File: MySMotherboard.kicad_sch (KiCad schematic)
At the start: 53 parts, among them SW1 RST, SW2 BTN, U1 MCP1640Cx-xCHY, U2 APE8865Y5-30-HF-3, U3 ATmega328PB-A, U4 AT25xxx, U5 RFM69HW, U6 ATSHA204A, U7 AP63205WU, U8 SP3481EN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

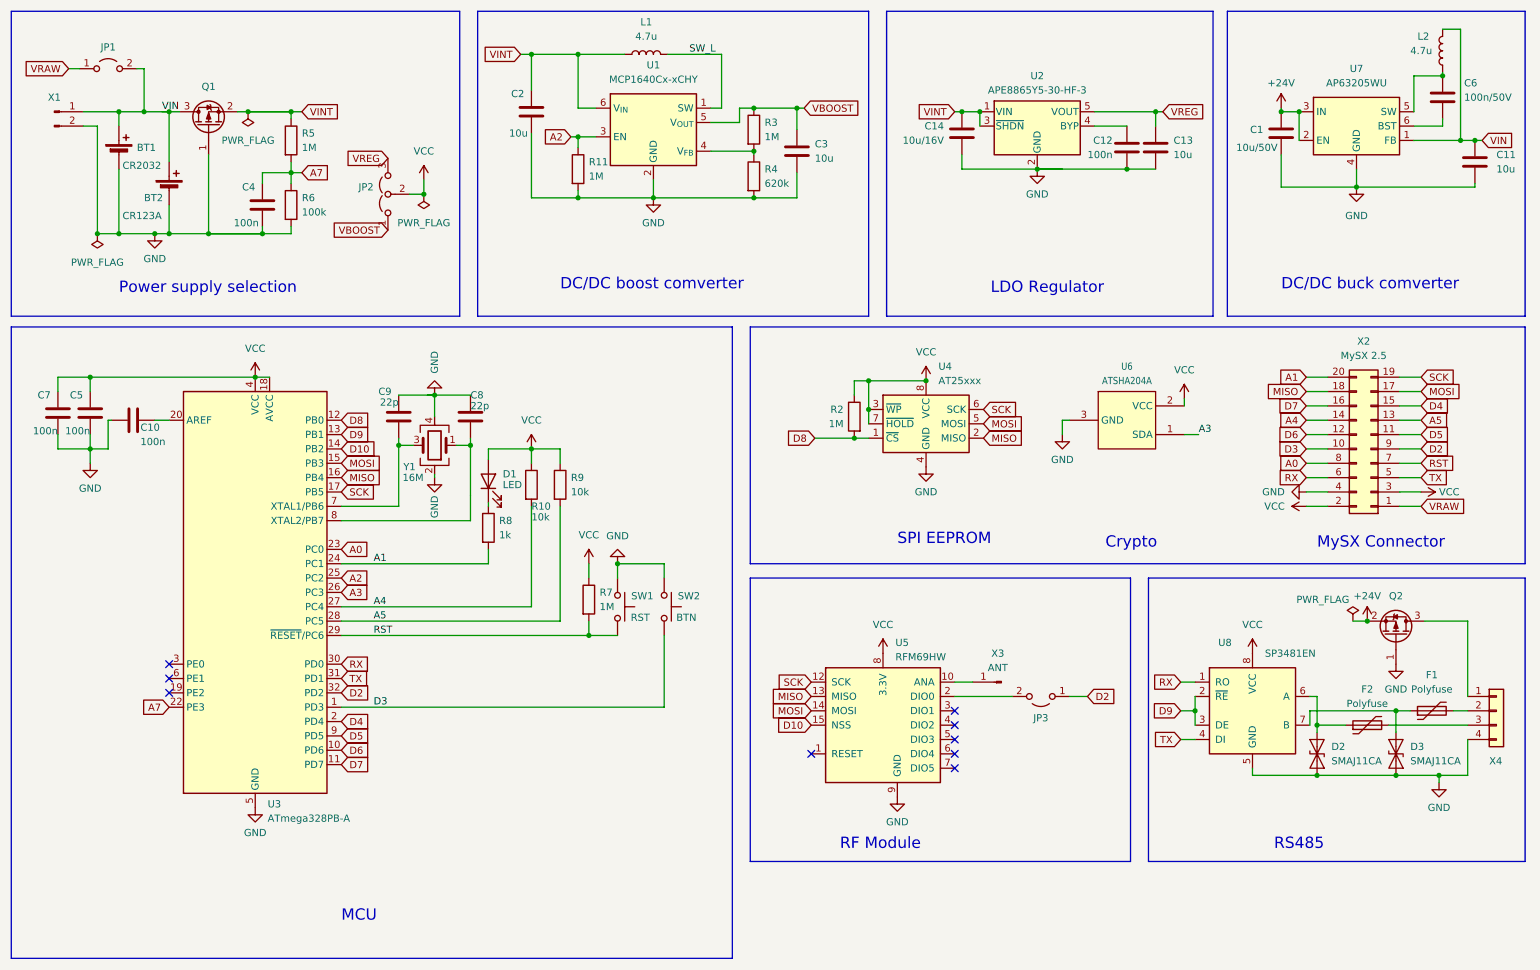
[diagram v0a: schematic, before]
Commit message: update to kicad 8
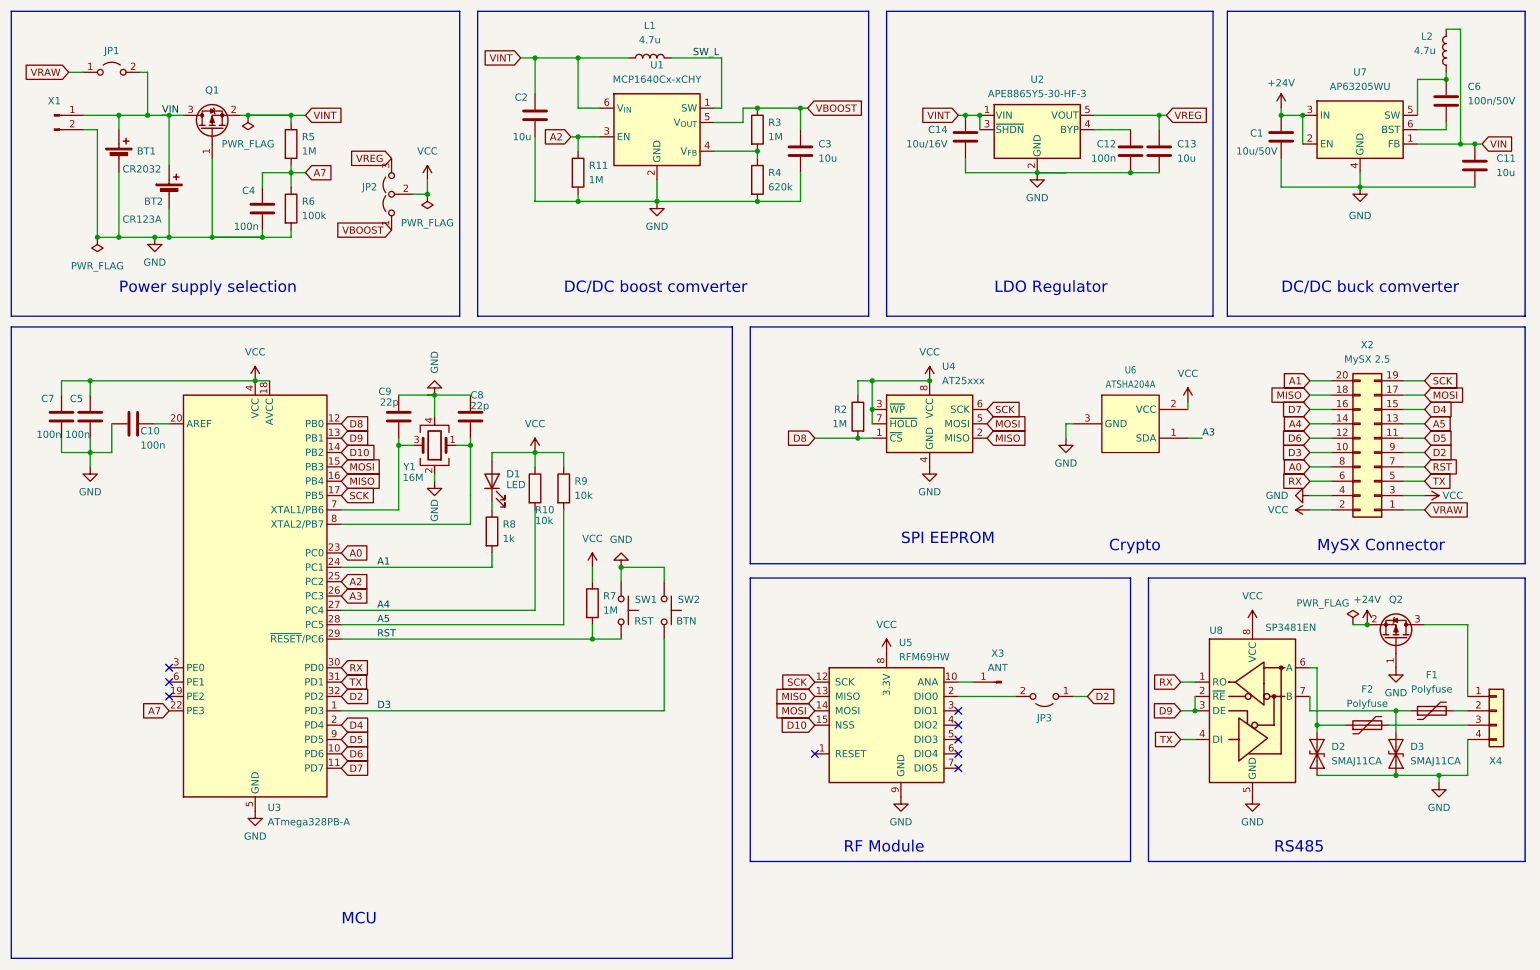
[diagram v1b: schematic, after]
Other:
- moved on the sheet: BT1, BT2, C1, C10, C11, C12, C13, C14, C2, C3, C4, C5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

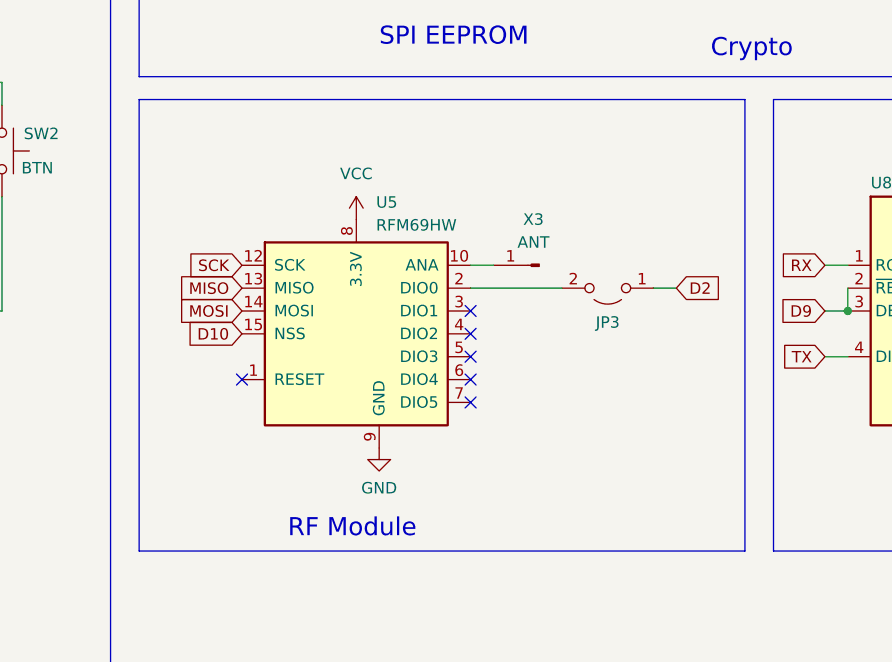
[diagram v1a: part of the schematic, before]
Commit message: add pull-up resistor for RFM69W NSS pin
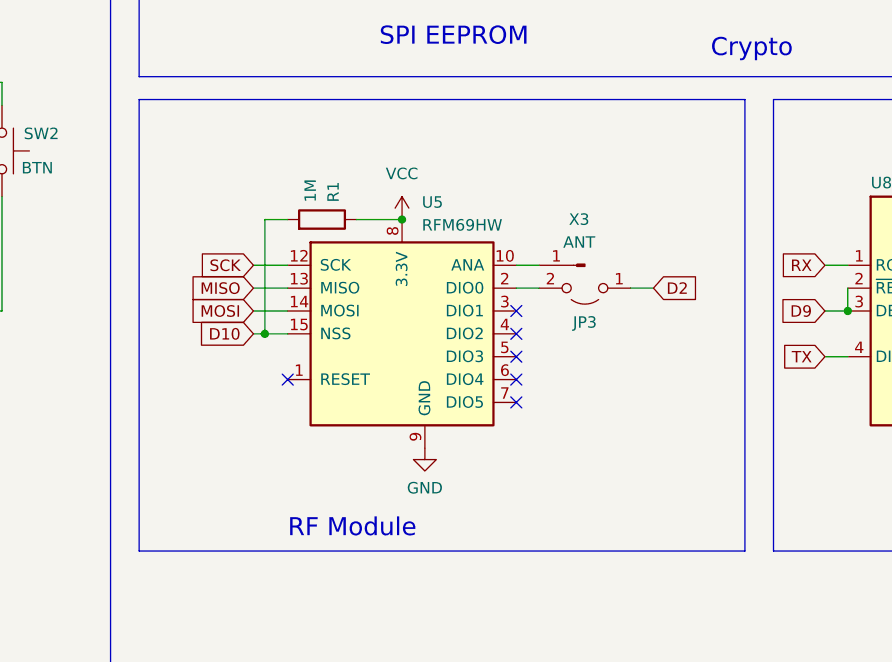
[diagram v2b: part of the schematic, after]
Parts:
- added R1: 1M, Resistor_SMD:R_0603_1608Metric, symbol Device:R
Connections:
- net D10: now also R1.2
- net VCC: now also R1.1
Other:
- moved on the sheet: JP3, U5, X3

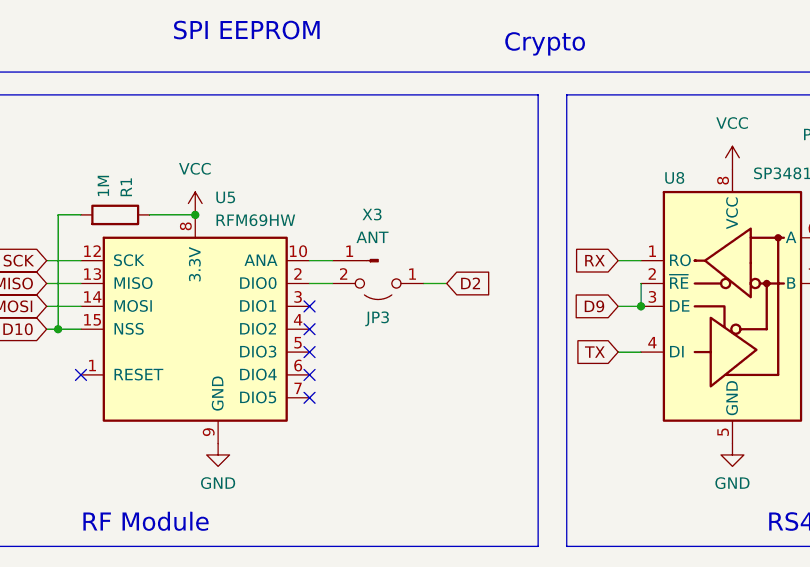
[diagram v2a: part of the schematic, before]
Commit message: add option to connect RFM69W irq to pin 3
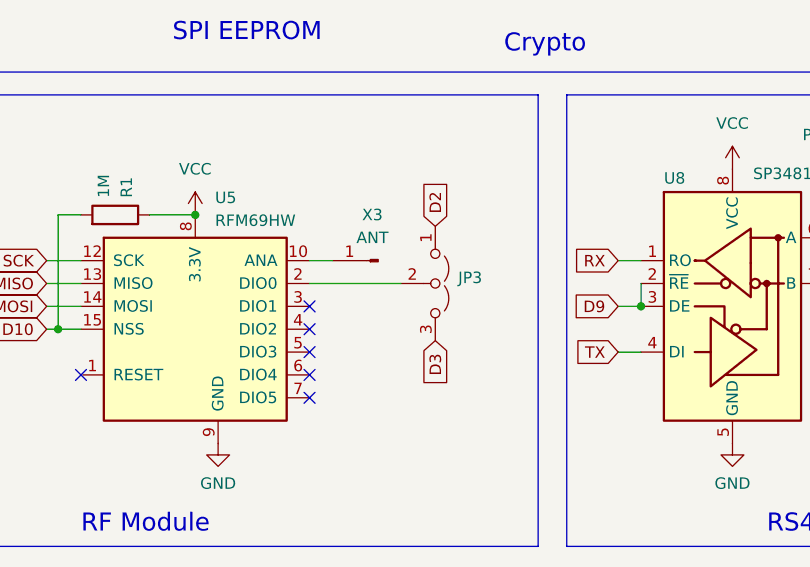
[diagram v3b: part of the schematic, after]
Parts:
- removed JP3: ~, Jumper:SolderJumper-2_P1.3mm_Open_RoundedPad1.0x1.5mm, symbol Jumper:Jumper_2_Open
- added JP3: ~, Jumper:SolderJumper-3_P1.3mm_Open_RoundedPad1.0x1.5mm, symbol Jumper:Jumper_3_Open
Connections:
- net D2: now also JP3.1 (A)
- net D3: now also JP3.3 (B)
- net at U5.2 (DIO0): now also JP3.2 (C)
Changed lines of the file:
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@@
 	(wire
 		(pts
-			(xy 199.39 134.62) (xy 201.93 134.62)
-		)
-		(stroke
-			(width 0)
-			(type default)
-		)
-	)
-	(wire
-		(pts
 			(xy 40.64 31.75) (xy 41.91 31.75)
 		)
@@
 	(wire
 		(pts
-			(xy 186.69 134.62) (xy 189.23 134.62)
+			(xy 186.69 134.62) (xy 196.85 134.62)
 		)
 		(stroke
@@
 	(global_label "D2"
 		(shape input)
-		(at 201.93 134.62 0)
+		(at 200.66 128.27 90)
 		(fields_autoplaced yes)
 		(effects
@@
 		)
 		(property "Intersheetrefs" "${INTERSHEET_REFS}"
-			(at 207.3947 134.62 0)
+			(at 200.66 122.8053 90)
 			(effects
 				(font
@@
 		)
 	)
+	(global_label "D3"
+		(shape input)
+		(at 200.66 140.97 270)
+		(fields_autoplaced yes)
+		(effects
+			(font
+				(size 1.27 1.27)
+			)
+			(justify right)
+		)
+		(property "Intersheetrefs" "${INTERSHEET_REFS}"
+			(at 200.66 146.4347 90)
+			(effects
+				(font
+					(size 1.27 1.27)
+				)
+				(justify right)
+				(hide yes)
+			)
+		)
+	)
 	(global_label "A5"
 		(shape input)
@@
 	)
 	(symbol
-		(lib_id "Jumper:Jumper_2_Open")
-		(at 194.31 134.62 180)
-		(unit 1)
-		(exclude_from_sim no)
-		(in_bom yes)
-		(on_board yes)
-		(dnp no)
-		(property "Reference" "JP3"
-			(at 194.31 138.43 0)
-			(effects
-				(font
-					(size 1.27 1.27)
-				)
-			)
-		)
-		(property "Value" "~"
-			(at 194.31 138.43 0)
-			(effects
-				(font
-					(size 1.27 1.27)
-				)
-			)
-		)
-		(property "Footprint" "Jumper:SolderJumper-2_P1.3mm_Open_RoundedPad1.0x1.5mm"
-			(at 194.31 134.62 0)
-			(effects
-				(font
-					(size 1.27 1.27)
-				)
-				(hide yes)
-			)
-		)
-		(property "Datasheet" "~"
-			(at 194.31 134.62 0)
-			(effects
-				(font
-					(size 1.27 1.27)
-				)
-				(hide yes)
-			)
-		)
-		(property "Description" ""
-			(at 194.31 134.62 0)
-			(effects
-				(font
-					(size 1.27 1.27)
-				)
-				(hide yes)
-			)
-		)
-		(pin "2"
-		)
-		(pin "1"
-		)
-		(instances
-			(project "MySMotherboard"
-				(path "/005ccf98-7ec2-4789-9497-178572c51999"
-					(reference "JP3")
-					(unit 1)
-				)
-			)
-		)
-	)
-	(symbol
 		(lib_id "Device:R")
 		(at 63.5 36.83 0)
@@
 					(unit 1)
 				)
+			)
+		)
+	)
+	(symbol
+		(lib_id "Jumper:Jumper_3_Open")
+		(at 200.66 134.62 270)
+		(unit 1)
+		(exclude_from_sim no)
+		(in_bom yes)
+		(on_board yes)
+		(dnp no)
+		(fields_autoplaced yes)
+		(property "Reference" "JP3"
+			(at 203.2 133.9849 90)
+			(effects
+				(font
+					(size 1.27 1.27)
+				)
+				(justify left)
+			)
+		)
+		(property "Value" "~"
+			(at 203.2 135.89 90)
+			(effects
+				(font
+					(size 1.27 1.27)
+				)
+				(justify left)
+			)
+		)
+		(property "Footprint" "Jumper:SolderJumper-3_P1.3mm_Open_RoundedPad1.0x1.5mm"
+			(at 200.66 134.62 0)
+			(effects
+				(font
+					(size 1.27 1.27)
+				)
+				(hide yes)
+			)
+		)
+		(property "Datasheet" "~"
+			(at 200.66 134.62 0)
+			(effects
+				(font
+					(size 1.27 1.27)
+				)
+				(hide yes)
+			)
+		)
+		(property "Description" ""
+			(at 200.66 134.62 0)
+			(effects
+				(font
+					(size 1.27 1.27)
+				)
+				(hide yes)
+			)
+		)
+		(pin "3"
+		)
+		(pin "1"
+		)
+		(pin "2"
+		)
+		(instances
+			(project "MySMotherboard"
+				(path "/005ccf98-7ec2-4789-9497-178572c51999"
+					(reference "JP3")
+					(unit 1)
+				)
